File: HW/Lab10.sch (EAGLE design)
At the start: 7 parts, among them Q1 IRLD024

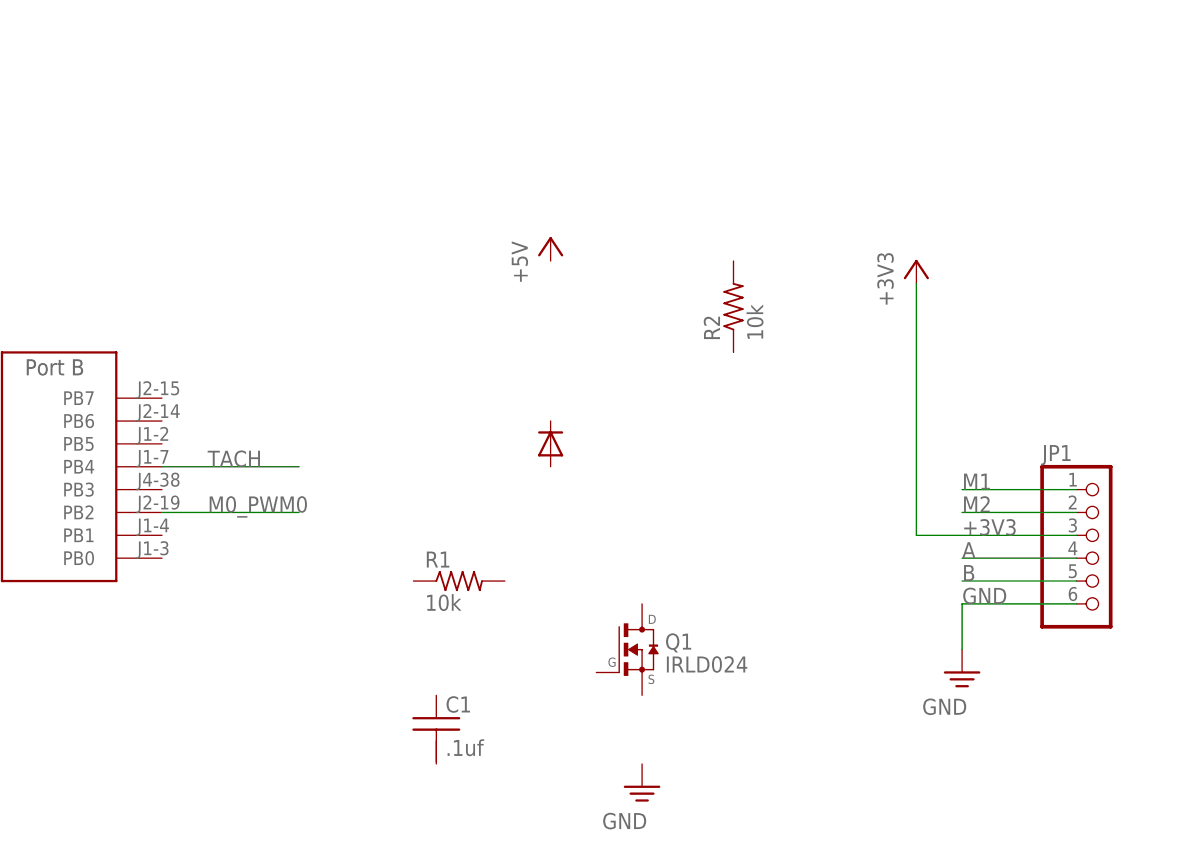
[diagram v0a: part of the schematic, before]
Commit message: finished schematic for motor and tachometer
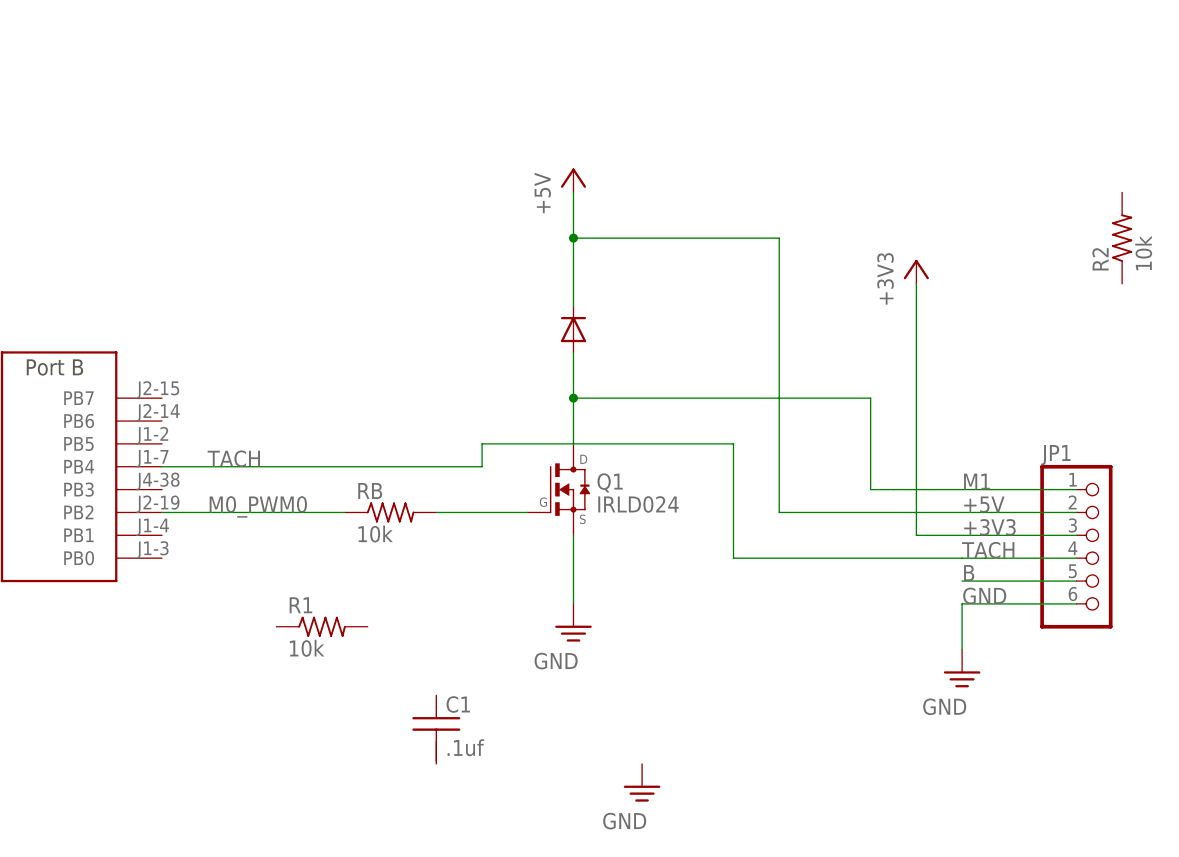
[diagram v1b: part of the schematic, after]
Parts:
- added RB: 10k, EE445L:RESISTOR0204/5
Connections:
- removed net A: JP1.4
- removed net M2: JP1.2
- new net +5V: D1.C, JP1.2
- new net N$1: Q1.G, RB.2
- net GND: now also Q1.S
- net M0_PWM0: now also RB.1
- net M1: now also D1.A, Q1.D
- net TACH: now also JP1.4
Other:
- moved on the sheet: Q1, R1, R2
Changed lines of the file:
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@@
 <?xml version="1.0" encoding="utf-8"?>
 <!DOCTYPE eagle SYSTEM "eagle.dtd">
-<eagle version="9.6.2">
+<eagle version="9.0.1">
 <drawing>
 <settings>
@@
 <part name="FRAME1" library="frames" deviceset="FRAME_A_L" device=""/>
 <part name="U$1" library="EE445L" deviceset="TM4C_BP" device=""/>
+<part name="RB" library="EE445L" deviceset="RESISTOR" device="0204/5" value="10k"/>
+<part name="SUPPLY3" library="EE445L" deviceset="GND" device=""/>
 </parts>
 <sheets>
@@
 </plain>
 <instances>
-<instance part="Q1" gate="G$1" x="157.48" y="111.76" smashed="yes">
-<attribute name="VALUE" x="160.02" y="109.22" size="1.778" layer="96"/>
-<attribute name="NAME" x="160.02" y="111.76" size="1.778" layer="95"/>
-</instance>
-<instance part="D1" gate="G$1" x="147.32" y="134.62" smashed="yes" rot="R90"/>
-<instance part="R1" gate="G$1" x="137.16" y="119.38" smashed="yes">
-<attribute name="NAME" x="133.35" y="120.8786" size="1.778" layer="95"/>
-<attribute name="VALUE" x="133.35" y="116.078" size="1.778" layer="96"/>
-</instance>
-<instance part="R2" gate="G$1" x="167.64" y="149.86" smashed="yes" rot="R90">
-<attribute name="NAME" x="166.1414" y="146.05" size="1.778" layer="95" rot="R90"/>
-<attribute name="VALUE" x="170.942" y="146.05" size="1.778" layer="96" rot="R90"/>
+<instance part="Q1" gate="G$1" x="149.86" y="129.54" smashed="yes">
+<attribute name="VALUE" x="152.4" y="127" size="1.778" layer="96"/>
+<attribute name="NAME" x="152.4" y="129.54" size="1.778" layer="95"/>
+</instance>
+<instance part="D1" gate="G$1" x="149.86" y="147.32" smashed="yes" rot="R90"/>
+<instance part="R1" gate="G$1" x="121.92" y="114.3" smashed="yes">
+<attribute name="NAME" x="118.11" y="115.7986" size="1.778" layer="95"/>
+<attribute name="VALUE" x="118.11" y="110.998" size="1.778" layer="96"/>
+</instance>
+<instance part="R2" gate="G$1" x="210.82" y="157.48" smashed="yes" rot="R90">
+<attribute name="NAME" x="209.3214" y="153.67" size="1.778" layer="95" rot="R90"/>
+<attribute name="VALUE" x="214.122" y="153.67" size="1.778" layer="96" rot="R90"/>
 </instance>
 <instance part="JP1" gate="A" x="208.28" y="121.92" smashed="yes">
@@
 <attribute name="VALUE" x="185.42" y="149.86" size="1.778" layer="96" rot="R90"/>
 </instance>
-<instance part="P+1" gate="1" x="147.32" y="157.48" smashed="yes">
-<attribute name="VALUE" x="144.78" y="152.4" size="1.778" layer="96" rot="R90"/>
+<instance part="P+1" gate="1" x="149.86" y="165.1" smashed="yes">
+<attribute name="VALUE" x="147.32" y="160.02" size="1.778" layer="96" rot="R90"/>
 </instance>
 <instance part="SUPPLY2" gate="GND" x="157.48" y="96.52" smashed="yes">
@@
 <instance part="U$1" gate="G$6" x="12.7" y="48.26" smashed="yes"/>
 <instance part="U$1" gate="G$7" x="12.7" y="20.32" smashed="yes"/>
+<instance part="RB" gate="G$1" x="129.54" y="127" smashed="yes">
+<attribute name="NAME" x="125.73" y="128.4986" size="1.778" layer="95"/>
+<attribute name="VALUE" x="125.73" y="123.698" size="1.778" layer="96"/>
+</instance>
+<instance part="SUPPLY3" gate="GND" x="149.86" y="114.3" smashed="yes">
+<attribute name="VALUE" x="145.415" y="109.601" size="1.778" layer="96"/>
+</instance>
 </instances>
 <busses>
@@
 <segment>
 <pinref part="JP1" gate="A" pin="1"/>
-<wire x1="205.74" y1="129.54" x2="193.04" y2="129.54" width="0.1524" layer="91"/>
+<wire x1="205.74" y1="129.54" x2="185.42" y2="129.54" width="0.1524" layer="91"/>
 <label x="193.04" y="129.54" size="1.778" layer="95"/>
-</segment>
-</net>
-<net name="M2" class="0">
-<segment>
-<pinref part="JP1" gate="A" pin="2"/>
-<wire x1="205.74" y1="127" x2="193.04" y2="127" width="0.1524" layer="91"/>
-<label x="193.04" y="127" size="1.778" layer="95"/>
-</segment>
-</net>
-<net name="A" class="0">
-<segment>
-<pinref part="JP1" gate="A" pin="4"/>
-<wire x1="205.74" y1="121.92" x2="193.04" y2="121.92" width="0.1524" layer="91"/>
-<label x="193.04" y="121.92" size="1.778" layer="95"/>
+<pinref part="Q1" gate="G$1" pin="D"/>
+<pinref part="D1" gate="G$1" pin="A"/>
+<wire x1="149.86" y1="144.78" x2="149.86" y2="139.7" width="0.1524" layer="91"/>
+<junction x="149.86" y="139.7"/>
+<wire x1="149.86" y1="139.7" x2="149.86" y2="134.62" width="0.1524" layer="91"/>
+<wire x1="149.86" y1="139.7" x2="182.88" y2="139.7" width="0.1524" layer="91"/>
+<wire x1="182.88" y1="139.7" x2="182.88" y2="129.54" width="0.1524" layer="91"/>
+<wire x1="185.42" y1="129.54" x2="182.88" y2="129.54" width="0.1524" layer="91"/>
 </segment>
 </net>
@@
 <wire x1="193.04" y1="111.76" x2="193.04" y2="116.84" width="0.1524" layer="91"/>
 </segment>
+<segment>
+<pinref part="Q1" gate="G$1" pin="S"/>
+<pinref part="SUPPLY3" gate="GND" pin="GND"/>
+<wire x1="149.86" y1="116.84" x2="149.86" y2="124.46" width="0.1524" layer="91"/>
+</segment>
 </net>
 <net name="+3V3" class="0">
@@
 <segment>
 <pinref part="U$1" gate="G$2" pin="PB2"/>
-<wire x1="104.14" y1="127" x2="119.38" y2="127" width="0.1524" layer="91"/>
+<wire x1="104.14" y1="127" x2="124.46" y2="127" width="0.1524" layer="91"/>
 <label x="109.22" y="127" size="1.778" layer="95"/>
+<pinref part="RB" gate="G$1" pin="1"/>
 </segment>
 </net>
@@
 <segment>
 <pinref part="U$1" gate="G$2" pin="PB4"/>
-<wire x1="104.14" y1="132.08" x2="119.38" y2="132.08" width="0.1524" layer="91"/>
 <label x="109.22" y="132.08" size="1.778" layer="95"/>
-</segment>
-</net>
+<wire x1="104.14" y1="132.08" x2="139.7" y2="132.08" width="0.1524" layer="91"/>
+<wire x1="139.7" y1="132.08" x2="139.7" y2="134.62" width="0.1524" layer="91"/>
+<wire x1="139.7" y1="134.62" x2="167.64" y2="134.62" width="0.1524" layer="91"/>
+<wire x1="167.64" y1="134.62" x2="167.64" y2="121.92" width="0.1524" layer="91"/>
+<pinref part="JP1" gate="A" pin="4"/>
+<wire x1="205.74" y1="121.92" x2="195.58" y2="121.92" width="0.1524" layer="91"/>
+<label x="193.04" y="121.92" size="1.778" layer="95"/>
+<wire x1="195.58" y1="121.92" x2="193.04" y2="121.92" width="0.1524" layer="91"/>
+<wire x1="167.64" y1="121.92" x2="193.04" y2="121.92" width="0.1524" layer="91"/>
+</segment>
+</net>
+<net name="N$1" class="0">
+<segment>
+<pinref part="RB" gate="G$1" pin="2"/>
+<pinref part="Q1" gate="G$1" pin="G"/>
+<wire x1="144.78" y1="127" x2="134.62" y2="127" width="0.1524" layer="91"/>
+</segment>
+</net>
+<net name="+5V" class="0">
+<segment>
+<pinref part="D1" gate="G$1" pin="C"/>
+<pinref part="P+1" gate="1" pin="+5V"/>
+<wire x1="149.86" y1="162.56" x2="149.86" y2="157.48" width="0.1524" layer="91"/>
+<junction x="149.86" y="157.48"/>
+<wire x1="149.86" y1="157.48" x2="149.86" y2="149.86" width="0.1524" layer="91"/>
+<wire x1="149.86" y1="157.48" x2="172.72" y2="157.48" width="0.1524" layer="91"/>
+<wire x1="172.72" y1="157.48" x2="172.72" y2="127" width="0.1524" layer="91"/>
+<pinref part="JP1" gate="A" pin="2"/>
+<label x="193.04" y="127" size="1.778" layer="95"/>
+<wire x1="172.72" y1="127" x2="205.74" y2="127" width="0.1524" layer="91"/>
+</segment>
+</net>

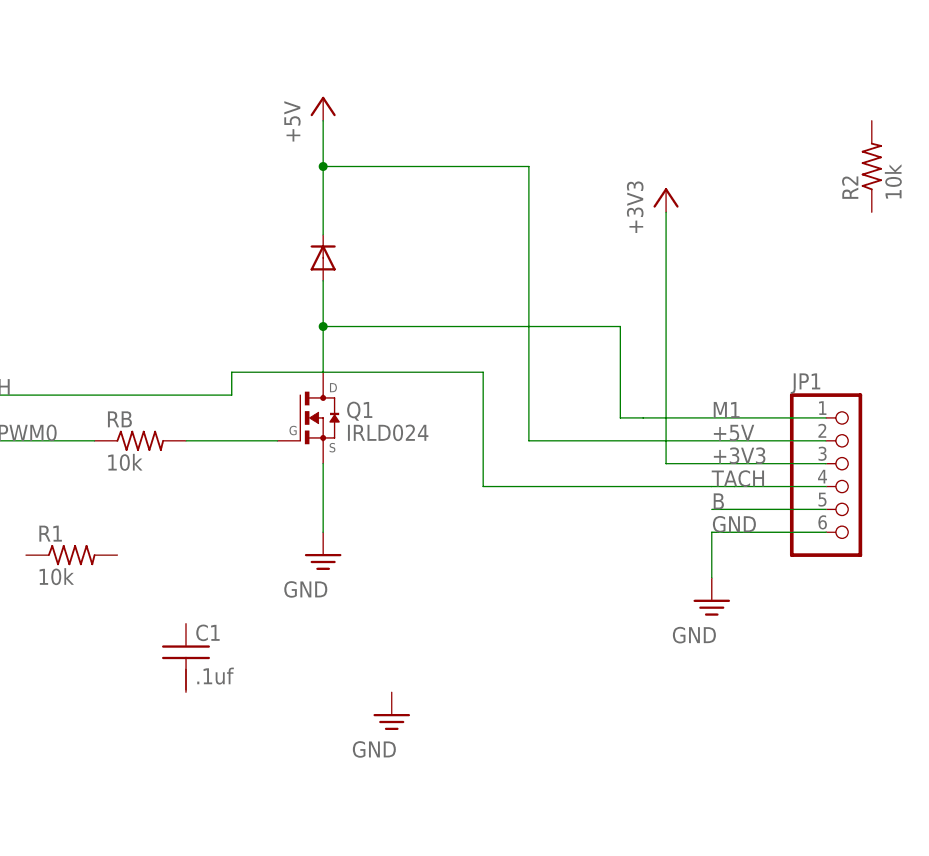
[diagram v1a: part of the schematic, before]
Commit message: put capacitor across DC motor terminals
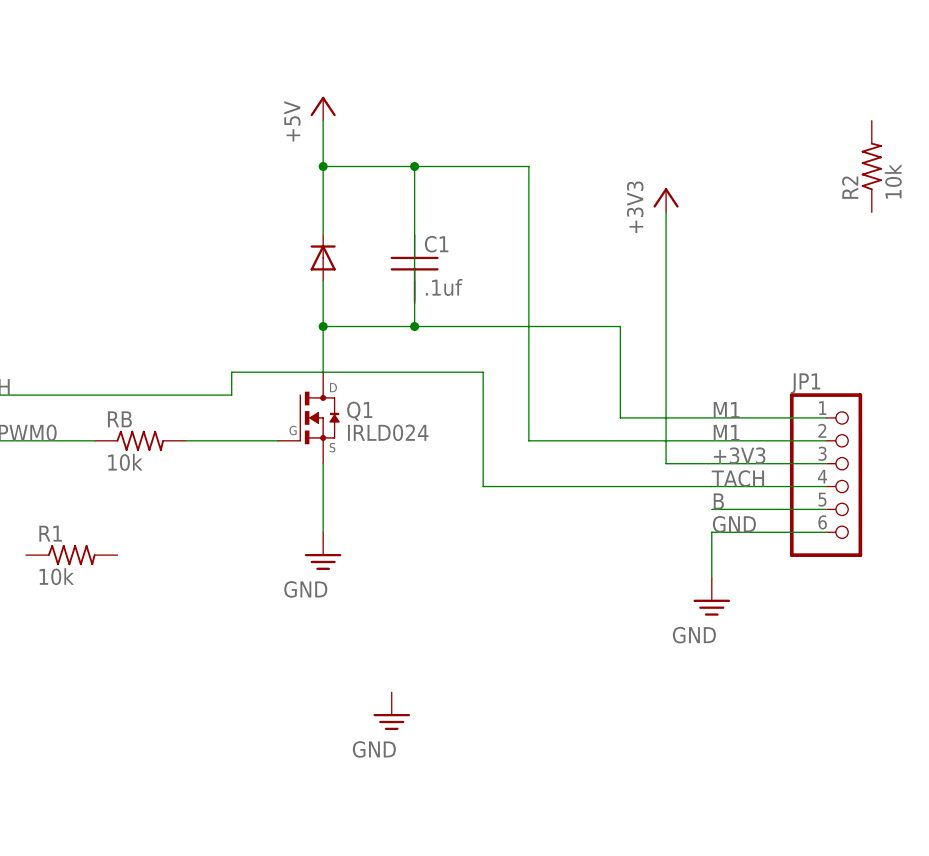
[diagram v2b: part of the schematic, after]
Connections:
- removed net +5V: D1.C, JP1.2
- net M1: now also C1.1, D1.C, JP1.2
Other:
- moved on the sheet: C1
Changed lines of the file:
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@@
 <attribute name="VALUE" x="153.035" y="91.821" size="1.778" layer="96"/>
 </instance>
-<instance part="C1" gate="G$1" x="134.62" y="104.14" smashed="yes">
-<attribute name="NAME" x="135.636" y="104.775" size="1.778" layer="95"/>
-<attribute name="VALUE" x="135.636" y="99.949" size="1.778" layer="96"/>
+<instance part="C1" gate="G$1" x="160.02" y="147.32" smashed="yes">
+<attribute name="NAME" x="161.036" y="147.955" size="1.778" layer="95"/>
+<attribute name="VALUE" x="161.036" y="143.129" size="1.778" layer="96"/>
 </instance>
 <instance part="FRAME1" gate="G$1" x="0" y="0" smashed="yes"/>
@@
 </busses>
 <nets>
-<net name="M1" class="0">
-<segment>
-<pinref part="JP1" gate="A" pin="1"/>
-<wire x1="205.74" y1="129.54" x2="185.42" y2="129.54" width="0.1524" layer="91"/>
-<label x="193.04" y="129.54" size="1.778" layer="95"/>
-<pinref part="Q1" gate="G$1" pin="D"/>
-<pinref part="D1" gate="G$1" pin="A"/>
-<wire x1="149.86" y1="144.78" x2="149.86" y2="139.7" width="0.1524" layer="91"/>
-<junction x="149.86" y="139.7"/>
-<wire x1="149.86" y1="139.7" x2="149.86" y2="134.62" width="0.1524" layer="91"/>
-<wire x1="149.86" y1="139.7" x2="182.88" y2="139.7" width="0.1524" layer="91"/>
-<wire x1="182.88" y1="139.7" x2="182.88" y2="129.54" width="0.1524" layer="91"/>
-<wire x1="185.42" y1="129.54" x2="182.88" y2="129.54" width="0.1524" layer="91"/>
-</segment>
-</net>
 <net name="B" class="0">
 <segment>
@@
 </segment>
 </net>
-<net name="+5V" class="0">
+<net name="M1" class="0">
 <segment>
 <pinref part="D1" gate="G$1" pin="C"/>
@@
 <junction x="149.86" y="157.48"/>
 <wire x1="149.86" y1="157.48" x2="149.86" y2="149.86" width="0.1524" layer="91"/>
-<wire x1="149.86" y1="157.48" x2="172.72" y2="157.48" width="0.1524" layer="91"/>
+<wire x1="149.86" y1="157.48" x2="160.02" y2="157.48" width="0.1524" layer="91"/>
+<wire x1="160.02" y1="157.48" x2="172.72" y2="157.48" width="0.1524" layer="91"/>
 <wire x1="172.72" y1="157.48" x2="172.72" y2="127" width="0.1524" layer="91"/>
 <pinref part="JP1" gate="A" pin="2"/>
 <label x="193.04" y="127" size="1.778" layer="95"/>
 <wire x1="172.72" y1="127" x2="205.74" y2="127" width="0.1524" layer="91"/>
+<junction x="160.02" y="157.48"/>
+<pinref part="C1" gate="G$1" pin="1"/>
+<wire x1="160.02" y1="157.48" x2="160.02" y2="149.86" width="0.1524" layer="91"/>
+<pinref part="JP1" gate="A" pin="1"/>
+<wire x1="205.74" y1="129.54" x2="182.88" y2="129.54" width="0.1524" layer="91"/>
+<label x="193.04" y="129.54" size="1.778" layer="95"/>
+<pinref part="Q1" gate="G$1" pin="D"/>
+<pinref part="D1" gate="G$1" pin="A"/>
+<wire x1="149.86" y1="144.78" x2="149.86" y2="139.7" width="0.1524" layer="91"/>
+<junction x="149.86" y="139.7"/>
+<wire x1="149.86" y1="139.7" x2="149.86" y2="134.62" width="0.1524" layer="91"/>
+<wire x1="149.86" y1="139.7" x2="160.02" y2="139.7" width="0.1524" layer="91"/>
+<wire x1="160.02" y1="139.7" x2="182.88" y2="139.7" width="0.1524" layer="91"/>
+<wire x1="182.88" y1="139.7" x2="182.88" y2="129.54" width="0.1524" layer="91"/>
+<junction x="160.02" y="139.7"/>
+<wire x1="160.02" y1="149.86" x2="160.02" y2="139.7" width="0.1524" layer="91"/>
 </segment>
 </net>

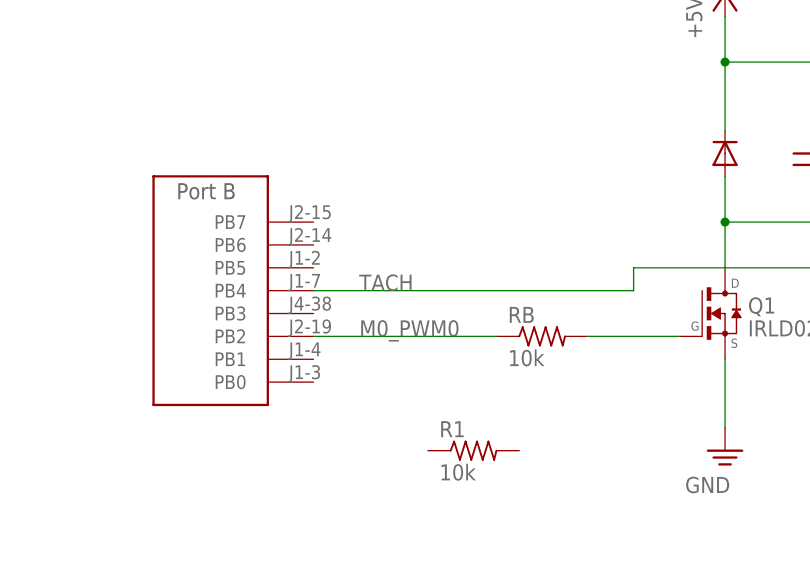
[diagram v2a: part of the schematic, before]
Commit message: changed M0PWM0 to PB6 instead of PB2
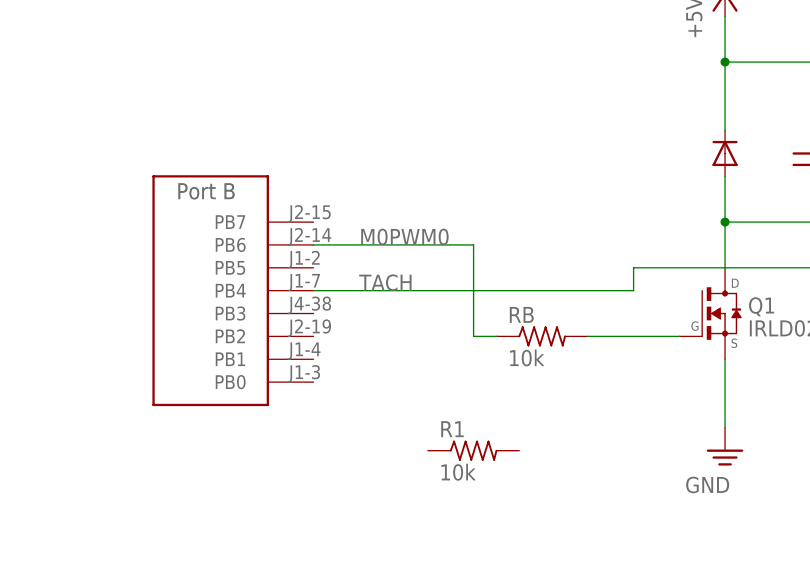
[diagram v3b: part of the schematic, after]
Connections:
- removed net M0_PWM0: RB.1, U$1G$2.PB2
- new net M0PWM0: RB.1, U$1G$2.PB6
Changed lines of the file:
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@@
-</segment>
-</net>
-<net name="M0_PWM0" class="0">
-<segment>
-<pinref part="U$1" gate="G$2" pin="PB2"/>
-<wire x1="104.14" y1="127" x2="124.46" y2="127" width="0.1524" layer="91"/>
-<label x="109.22" y="127" size="1.778" layer="95"/>
-<pinref part="RB" gate="G$1" pin="1"/>
 </segment>
 </net>
@@
 </segment>
 </net>
+<net name="M0PWM0" class="0">
+<segment>
+<pinref part="U$1" gate="G$2" pin="PB6"/>
+<wire x1="104.14" y1="137.16" x2="121.92" y2="137.16" width="0.1524" layer="91"/>
+<pinref part="RB" gate="G$1" pin="1"/>
+<wire x1="121.92" y1="137.16" x2="121.92" y2="127" width="0.1524" layer="91"/>
+<wire x1="121.92" y1="127" x2="124.46" y2="127" width="0.1524" layer="91"/>
+<label x="109.22" y="137.16" size="1.778" layer="95"/>
+</segment>
+</net>

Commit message: Updated HW schematic
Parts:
- removed R1: 10k, EE445L:RESISTOR0204/5
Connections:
- new net M2: D1.C, JP1.2
- net +3V3: now also C1.1, R2.2
- net GND: now also C1.2
- net M1: no longer C1.1, D1.C, JP1.2
- net TACH: now also R2.1
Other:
- moved on the sheet: C1, Q1, R2, RB
